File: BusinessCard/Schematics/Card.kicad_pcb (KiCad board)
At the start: 2 copper layers, 88.1 x 50.2 mm, 18 parts, among them J1 USB_A, J2 System, J3 ExpansionPort, J4 CapPad1, J5 CapPad2, J6 Programming Port, U1 CH552T

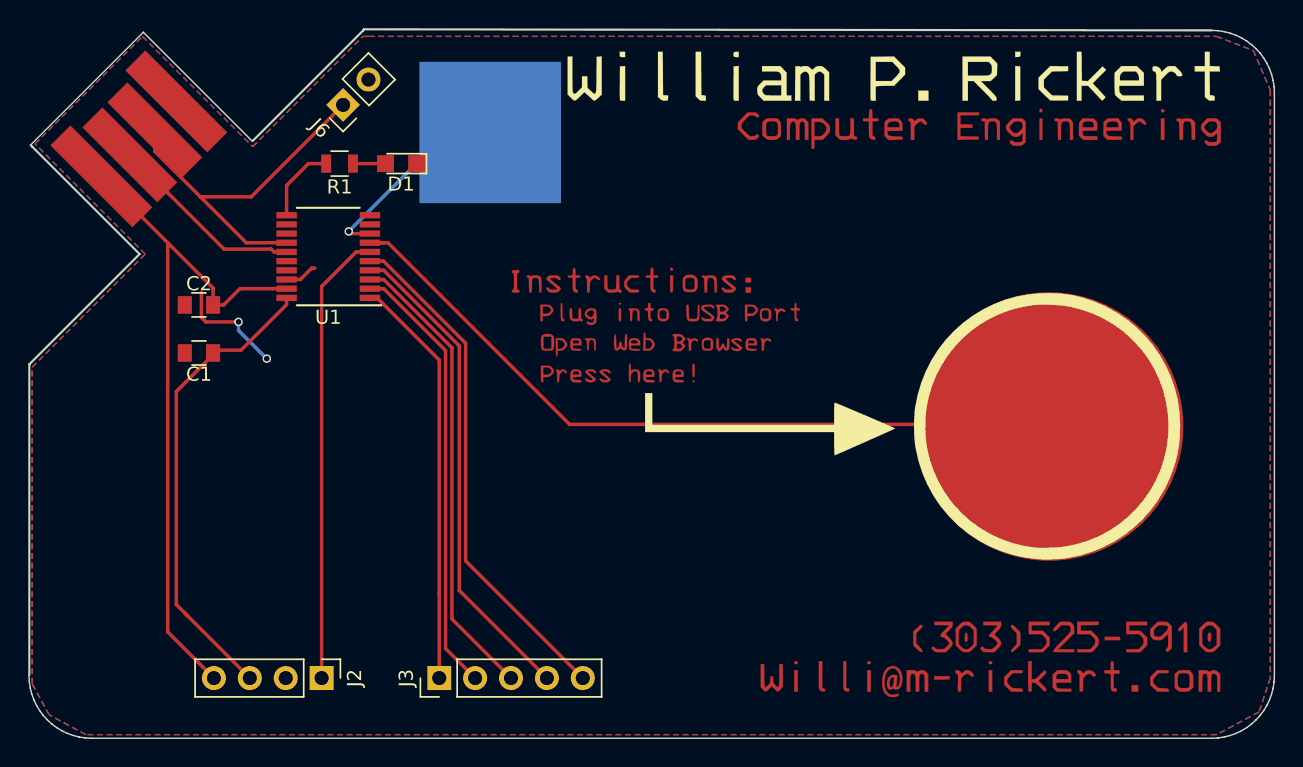
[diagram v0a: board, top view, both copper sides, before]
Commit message: Cant believe I had D+ and D- mixed...
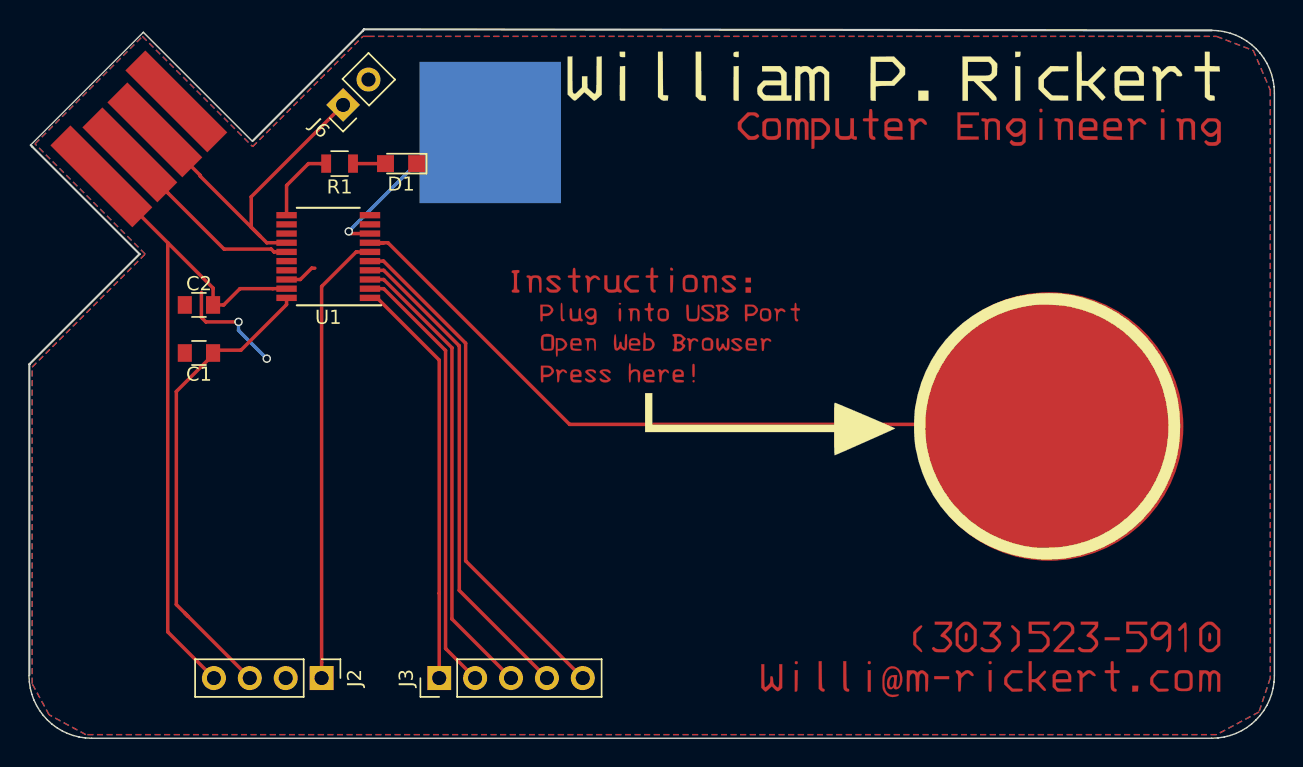
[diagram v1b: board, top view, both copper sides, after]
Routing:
- net D+: track 26.3 -> 25.3 mm
